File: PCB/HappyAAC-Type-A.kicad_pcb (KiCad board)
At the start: 2 copper layers, 79.9 x 48.6 mm, 31 parts, among them J1 IR_RX, J10 SPEAKER, J11 ICSP, J12 TFT_LCD, J13 SDCard_Conn, J14_GPIO1 Conn_03x04_Odd_Even_VSG, J15_GPIO2 Conn_03x04_Odd_Even_VSG, J16_GPIO3 Conn_03x04_Odd_Even_VSG, J17_GPIO4 Conn_03x04_Odd_Even_VSG, J18 AudioJack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

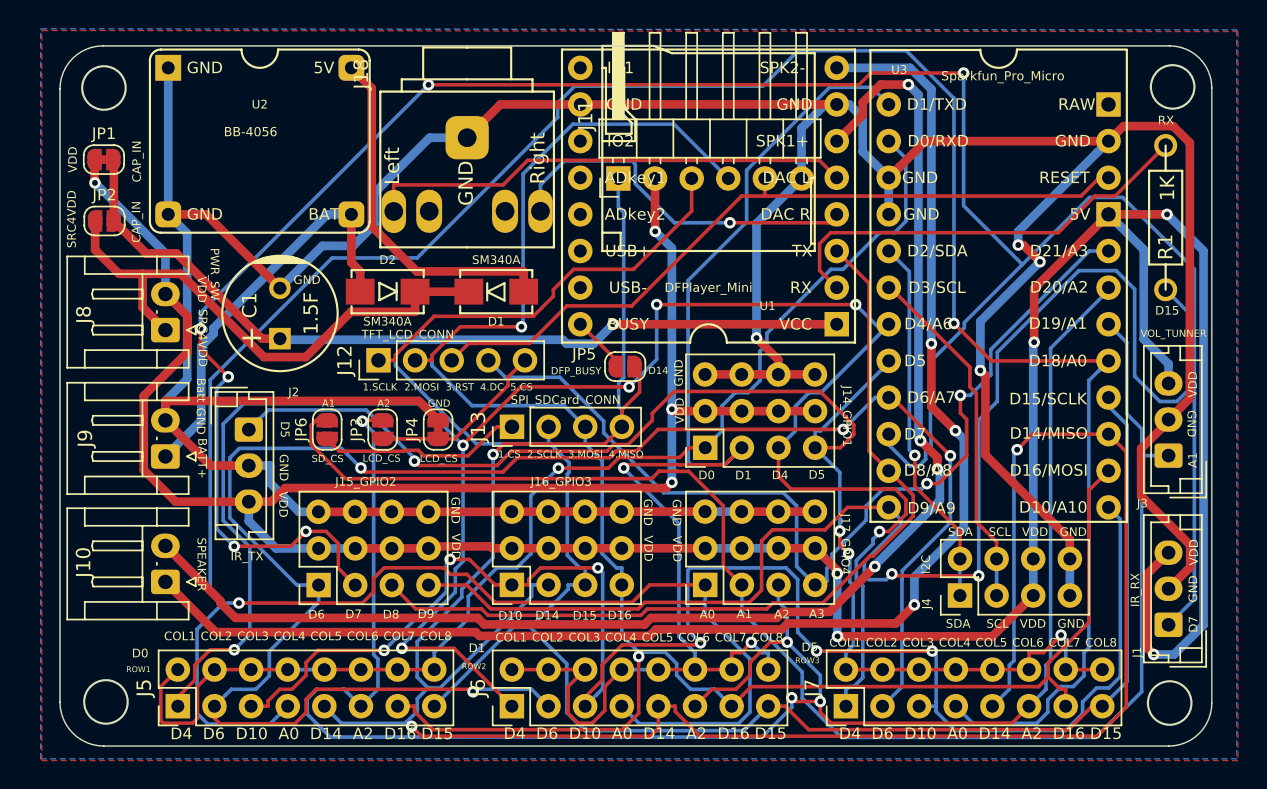
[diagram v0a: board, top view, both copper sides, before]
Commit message: Update J8 PWR_SW ,J9 BATT_SW ,J10 SPEAKER footprint association to JST_XH_S2B-XH-A_1x02_P2.50mm_Horizontal Update PCB routing
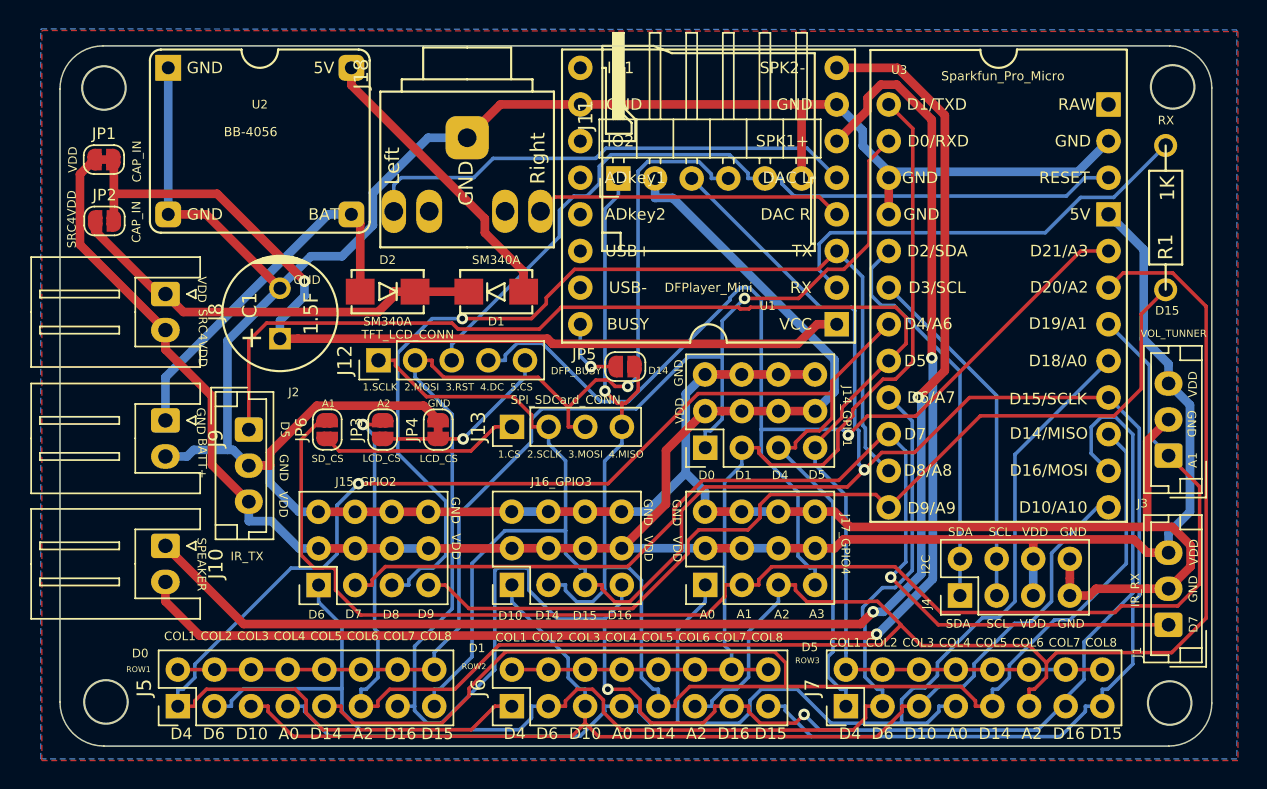
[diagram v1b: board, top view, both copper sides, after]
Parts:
- J10, J8, J9: footprint Connector_JST:JST_EH_S2B-EH_1x02_P2.50mm_Horizontal -> Connector_JST:JST_XH_S2B-XH-A_1x02_P2.50mm_Horizontal
- moved J10 2.50 mm to (67.4, 61.5), turned to 270 degrees
- moved J8 2.50 mm to (67.4, 44.0), turned to 270 degrees
- moved J9 2.50 mm to (67.4, 52.8), turned to 270 degrees
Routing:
- net /A0: track 212.8 -> 94.9 mm, vias 2 -> 0
- net /D7: track 165.7 -> 73.5 mm, vias 6 -> 1
- net VDD: track 245.9 -> 167.9 mm, vias 9 -> 0
- net GND: track 286.8 -> 238.2 mm, vias 4 -> 0
- net /COL2: track 125.0 -> 86.5 mm, vias 4 -> 0
- net /COL5: track 170.5 -> 136.5 mm, vias 3 -> 1
- net /D9: track 99.3 -> 65.8 mm, vias 2 -> 0
- net /COL3: track 112.5 -> 82.5 mm, vias 6 -> 0
- net /COL1: track 143.8 -> 117.1 mm, vias 7 -> 1
- net /COL8: track 139.0 -> 165.0 mm, vias 0 -> 1
- net /COL7: track 140.1 -> 166.1 mm, vias 2 -> 3
- net /D1: track 92.5 -> 69.0 mm, vias 2 -> 0
- net /A2: track 130.9 -> 141.1 mm, vias 4 -> 1
- net /D8: track 60.5 -> 70.6 mm, vias 0 -> 1
- net /A3: track 67.5 -> 76.1 mm, vias 2 -> 1
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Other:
- board text added: "HappyAAC type-A Rev-2d 2021.0607-1"
- board text removed: "HappyAAC Type-A Rev-2c 2021.0420-1"

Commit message: 1. Fix wrong PCB text for R1 (D15-->D9) on F.SilkS and B.SilkS 2. Update PCB version text to 2021.0611-1
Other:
- board text added: "HappyAAC type-A Rev-2d 2021.0611-1"
- board text removed: "HappyAAC type-A Rev-2d 2021.0607-1"
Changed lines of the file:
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@@
       (effects (font (size 1 1) (thickness 0.15)))
     )
-    (pad 1 thru_hole roundrect (at 0 0 270) (size 1.7 2) (drill 1) (layers *.Cu *.Mask) (roundrect_rratio 0.147059)
+    (pad 1 thru_hole roundrect (at 0 0 270) (size 1.7 2) (drill 1) (layers *.Cu *.Mask) (roundrect_rratio 0.1470588235294118)
       (net 4 /SRC_FOR_VDD))
     (pad 2 thru_hole oval (at 2.5 0 270) (size 1.7 2) (drill 1) (layers *.Cu *.Mask)
@@
       (effects (font (size 1 1) (thickness 0.15)))
     )
-    (pad 1 thru_hole roundrect (at 0 0 270) (size 1.7 2) (drill 1) (layers *.Cu *.Mask) (roundrect_rratio 0.147059)
+    (pad 1 thru_hole roundrect (at 0 0 270) (size 1.7 2) (drill 1) (layers *.Cu *.Mask) (roundrect_rratio 0.1470588235294118)
       (net 5 +BATT))
     (pad 2 thru_hole oval (at 2.5 0 270) (size 1.7 2) (drill 1) (layers *.Cu *.Mask)
@@
     (pad 2 thru_hole oval (at 2.5 0 270) (size 1.7 2) (drill 1) (layers *.Cu *.Mask)
       (net 17 /SPK1))
-    (pad 1 thru_hole roundrect (at 0 0 270) (size 1.7 2) (drill 1) (layers *.Cu *.Mask) (roundrect_rratio 0.147059)
+    (pad 1 thru_hole roundrect (at 0 0 270) (size 1.7 2) (drill 1) (layers *.Cu *.Mask) (roundrect_rratio 0.1470588235294118)
       (net 16 /SPK2))
     (model ${KISYS3DMOD}/Connector_JST.3dshapes/JST_XH_S2B-XH-A_1x02_P2.50mm_Horizontal.wrl
@@
     (effects (font (size 0.5 0.5) (thickness 0.1)) (justify mirror))
   )
-  (gr_text "HappyAAC type-A Rev-2d\n2021.0607-1" (at 125.26264 28.40228) (layer B.SilkS)
+  (gr_text "HappyAAC type-A Rev-2d\n2021.0611-1" (at 125.26264 28.40228) (layer B.SilkS)
     (effects (font (size 0.7 0.7) (thickness 0.15) italic) (justify mirror))
   )
@@
     (effects (font (size 0.6 0.6) (thickness 0.1)) (justify mirror))
   )
-  (gr_text D15 (at 136.91108 45.15612) (layer F.SilkS)
-    (effects (font (size 0.6 0.6) (thickness 0.1)))
-  )
-  (gr_text D15 (at 136.7155 45.3898) (layer B.SilkS)
+  (gr_text D9 (at 136.91108 45.15612) (layer F.SilkS)
+    (effects (font (size 0.6 0.6) (thickness 0.1)))
+  )
+  (gr_text D9 (at 136.7155 45.3898) (layer B.SilkS)
     (effects (font (size 0.8 0.8) (thickness 0.1)) (justify mirror))
   )

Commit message: 1. Fix footprint of J9 - battery connector, to keep connector's pin defination as text labels printed on the board. 2. Fix footprint of ICSP connector, let it's SilkS shape shows on the back side. 3. Fix footprint of U2 - BB-4056, enlarge it's pad size to help soldering. 4. Update zip package of gerber files. 5. Update pdf file of schematic.
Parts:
- J10, J8, J9: footprint Connector_JST:JST_XH_S2B-XH-A_1x02_P2.50mm_Horizontal -> footprintLib:PEC-2503-2H.JST_XH_S2B-XH-A_1x02_P2.50mm_Horizontal
- J11: footprint footprintLib:PinHeader_1x06_P2.54mm_Horizontal -> footprintLib:ICSP_PinHeader_1x06_P2.54mm_Horizontal
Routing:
- net /SPK2: track 97.6 -> 134.5 mm, vias 2 -> 0
- net /SPK1: track 98.8 -> 68.2 mm, vias 2 -> 0
- net /COL1: track 117.1 -> 86.5 mm, vias 1 -> 0
- net /COL8: track 165.0 -> 139.4 mm, vias 1 -> 0
- net /COL7: track 166.1 -> 143.1 mm, vias 3 -> 1
- net /A2: track 141.1 -> 120.3 mm
- net /A3: track 76.1 -> 94.9 mm
- net /D5: track 99.1 -> 83.6 mm
- net /A1: track 100.0 -> 85.3 mm, vias 0 -> 1
- net +BATT: track 26.2 -> 38.7 mm
- net /COL5: track 136.5 -> 126.3 mm, vias 1 -> 2
- net /D8: track 70.6 -> 79.2 mm
- net /A0: track 94.9 -> 86.3 mm, vias 0 -> 1
- net /D3: track 24.4 -> 31.1 mm
- net /COL2: track 86.5 -> 79.9 mm, vias 0 -> 2
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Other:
- board text added: "Battery"
- board text added: "HappyAAC type-A Rev-0.2e 2021/08/02-1"
- board text added: "SPK1"
- board text added: "SPK2"
- board text removed: "Batt"
- board text removed: "HappyAAC type-A Rev-2d 2021.0611-1"
- board text removed: "JP1"
- board text removed: "JP2"
